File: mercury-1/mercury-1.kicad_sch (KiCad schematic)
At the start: 76 parts, among them J1 +22.2V Logic Battery Array, J2 +14.4V Drivetrain Battery Arr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, J3 +22.2V A/S Battery Array, J4 Jetson, J5 POE Injector, J6 Network Switch, J7 P-20-90-PRO-121-B, J8 P-20-90-PRO-121-B, K1 200A Relay 12V Coil, K2 200A Relay 12V Coil, K3 200A Relay 12V Coil, K4 200A Relay 12V Coil, K5 200A Relay 12V Coil, K6 200A Relay 12V Coil, K7 200A Relay 12V Coil, K8 200A Relay 12V Coil, M1 Yellowjacket 5203, M10 NEO_Brushless_Motor, M2 FGA-32124500-G1166, M3 FGA-32124500-G1166, M4 CN-PA36-38244500-G369, M5 NEO_Brushless_Motor, M6 NEO_Brushless_Motor, M7 NEO_Brushless_Motor, M8 NEO_Brushless_Motor, M9 NEO_Brushless_Motor, SW1 SW_SPDT_321, U1 UVLO Relay, U10 MAX6675 Breakout, U11 MAX6675 Breakout, U12 MAX6675 Breakout, U13 MAX6675 Breakout, U14 MAX6675 Breakout, U15 RoboClaw_2x7A, U16 RoboClaw_2x7A, U18 ODESC_V4.2, U19 ODESC_V4.2, U2 Buck Converter, U20 ODESC_V4.2, U21 ODESC_V4.2, U22 ODESC_V4.2, U23 ODESC_V4.2, U24 5k (8mm Bore), U25 5k (8mm Bore), U26 5k (8mm Bore), U3 Buck Converter, U4 UVLO Relay, U5 Logic Relay, U6 Logic Relay, U7 UVLO Relay, U8 RASPBERRY_PI_4B_4GB, U9 MAX6675 Breakout

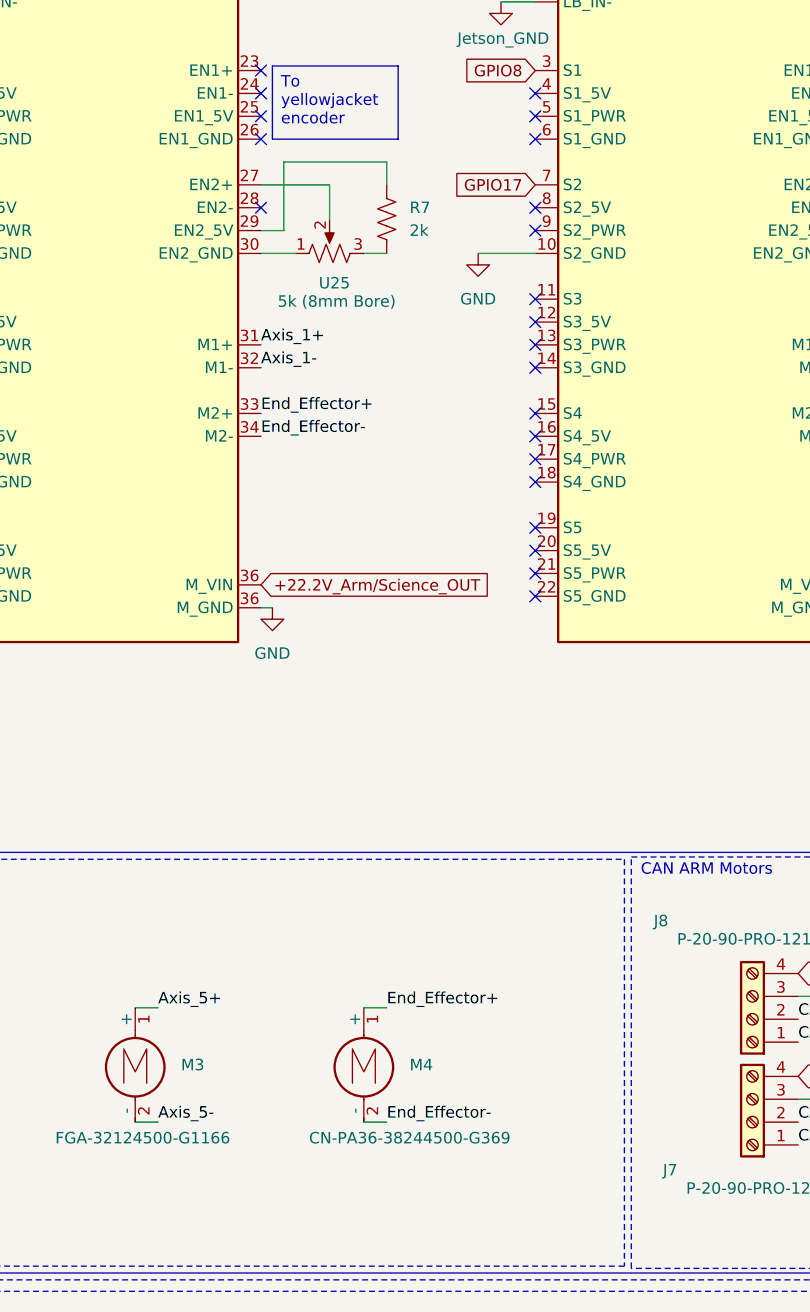
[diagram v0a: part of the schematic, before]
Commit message: changed end effector yo yellowjacket
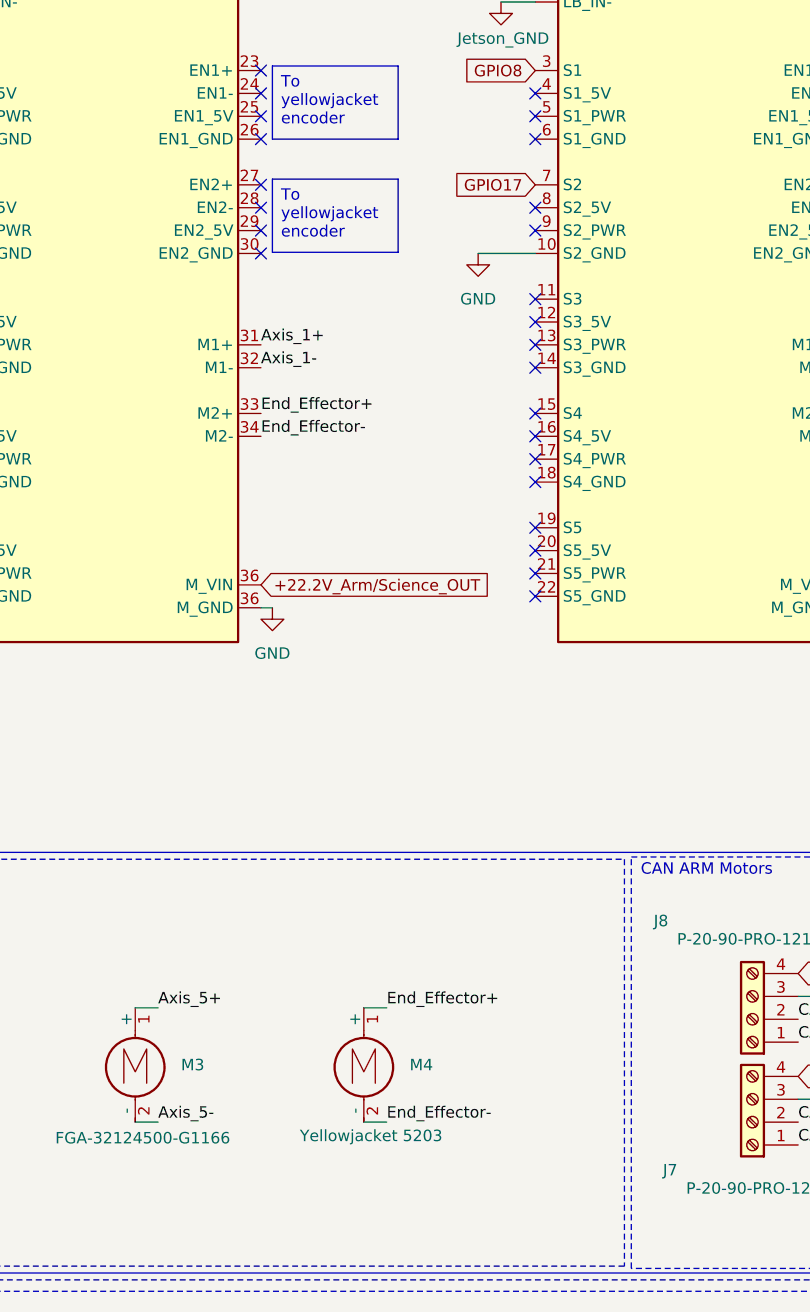
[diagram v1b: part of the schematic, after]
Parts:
- removed M4: CN-PA36-38244500-G369, symbol logic_board:CN-PA36-38244500-G369
- removed R7: 2k, symbol Device:R_US
- removed U25: 5k (8mm Bore), symbol logic_board:NP32HS
- added M4: Yellowjacket 5203, symbol logic_board:Yellowjacket 5203
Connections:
- net End_Effector+: now also M4.1 (+)
- net End_Effector-: now also M4.2 (-)
- no-connect marks 133 -> 136
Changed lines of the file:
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@@
 		)
 	)
+	(text_box "To yellowjacket encoder"
+		(exclude_from_sim no)
+		(at 184.15 283.845 0)
+		(size 13.97 8.128)
+		(margins 0.9525 0.9525 0.9525 0.9525)
+		(stroke
+			(width 0)
+			(type solid)
+		)
+		(fill
+			(type none)
+		)
+		(effects
+			(font
+				(size 1.27 1.27)
+			)
+			(justify left top)
+		)
+	)
 	(text_box "Use this guide to wire using Pyserial"
 		(exclude_from_sim no)
@@
 	)
 	(no_connect
+		(at 182.88 284.48)
+	)
+	(no_connect
 		(at 527.05 254)
 	)
@@
 	)
 	(no_connect
+		(at 182.88 289.56)
+	)
+	(no_connect
 		(at 496.57 212.09)
 	)
@@
 	)
 	(no_connect
+		(at 182.88 292.1)
+	)
+	(no_connect
 		(at 73.025 294.64)
 	)
@@
 		)
 	)
-	(wire
-		(pts
-			(xy 182.88 292.1) (xy 186.69 292.1)
-		)
-		(stroke
-			(width 0)
-			(type default)
-		)
-	)
 	(polyline
 		(pts
@@
 	(wire
 		(pts
-			(xy 182.88 289.56) (xy 185.42 289.56)
-		)
-		(stroke
-			(width 0)
-			(type default)
-		)
-	)
-	(wire
-		(pts
 			(xy 50.8 379.73) (xy 66.04 379.73)
 		)
@@
 	(wire
 		(pts
-			(xy 185.42 281.94) (xy 196.85 281.94)
-		)
-		(stroke
-			(width 0)
-			(type default)
-		)
-	)
-	(wire
-		(pts
 			(xy 199.39 173.99) (xy 208.28 173.99)
 		)
@@
 	(wire
 		(pts
-			(xy 194.31 292.1) (xy 196.85 292.1)
-		)
-		(stroke
-			(width 0)
-			(type default)
-		)
-	)
-	(wire
-		(pts
 			(xy 208.28 66.04) (xy 208.28 81.28)
 		)
@@
 	(wire
 		(pts
-			(xy 190.5 288.29) (xy 190.5 284.48)
-		)
-		(stroke
-			(width 0)
-			(type default)
-		)
-	)
-	(wire
-		(pts
-			(xy 185.42 281.94) (xy 185.42 289.56)
-		)
-		(stroke
-			(width 0)
-			(type default)
-		)
-	)
-	(wire
-		(pts
 			(xy 393.7 30.48) (xy 393.7 33.02)
 		)
@@
 	(wire
 		(pts
-			(xy 190.5 284.48) (xy 182.88 284.48)
-		)
-		(stroke
-			(width 0)
-			(type default)
-		)
-	)
-	(wire
-		(pts
 			(xy 251.46 269.24) (xy 251.46 276.86)
 		)
@@
 	(wire
 		(pts
-			(xy 196.85 281.94) (xy 196.85 284.48)
-		)
-		(stroke
-			(width 0)
-			(type default)
-		)
-	)
-	(wire
-		(pts
 			(xy 248.92 289.56) (xy 251.46 289.56)
 		)
@@
 	)
 	(symbol
+		(lib_id "logic_board:Yellowjacket 5203")
+		(at 194.31 381 0)
+		(unit 1)
+		(exclude_from_sim no)
+		(in_bom yes)
+		(on_board yes)
+		(dnp no)
+		(property "Reference" "M4"
+			(at 199.39 382.2699 0)
+			(effects
+				(font
+					(size 1.27 1.27)
+				)
+				(justify left)
+			)
+		)
+		(property "Value" "Yellowjacket 5203"
+			(at 187.198 390.144 0)
+			(effects
+				(font
+					(size 1.27 1.27)
+				)
+				(justify left)
+			)
+		)
+		(property "Footprint" ""
+			(at 194.31 383.286 0)
+			(effects
+				(font
+					(size 1.27 1.27)
+				)
+				(hide yes)
+			)
+		)
+		(property "Datasheet" "https://www.gobilda.com/5203-series-yellow-jacket-planetary-gear-motor-19-2-1-ratio-24mm-length-8mm-rex-shaft-312-rpm-3-3-5v-encoder/?srsltid=AfmBOop0hJPw3SFHkwtuK_eQ_aN3VPcP46iypOMregJbB3z72pbZtZjr"
+			(at 194.31 383.286 0)
+			(effects
+				(font
+					(size 1.27 1.27)
+				)
+				(hide yes)
+			)
+		)
+		(property "Description" "Yellowjacket 5203"
+			(at 194.31 381 0)
+			(effects
+				(font
+					(size 1.27 1.27)
+				)
+				(hide yes)
+			)
+		)
+		(pin "1"
+		)
+		(pin "2"
+		)
+		(instances
+			(project "mercury-1"
+				(path "/1b548578-061f-412b-9a17-10125f836cd9"
+					(reference "M4")
+					(unit 1)
+				)
+			)
+		)
+	)
+	(symbol
 		(lib_id "logic_board:MAX6675_Breakout")
 		(at 285.75 176.53 0)
@@
 	)
 	(symbol
-		(lib_id "logic_board:NP32HS")
-		(at 190.5 292.1 90)
-		(unit 1)
-		(exclude_from_sim no)
-		(in_bom yes)
-		(on_board yes)
-		(dnp no)
-		(property "Reference" "U25"
-			(at 192.786 295.402 90)
-			(effects
-				(font
-					(size 1.27 1.27)
-				)
-				(justify left)
-			)
-		)
-		(property "Value" "5k (8mm Bore)"
-			(at 197.866 297.434 90)
-			(effects
-				(font
-					(size 1.27 1.27)
-				)
-				(justify left)
-			)
-		)
-		(property "Footprint" ""
-			(at 190.5 292.1 0)
-			(effects
-				(font
-					(size 1.27 1.27)
-				)
-				(hide yes)
-			)
-		)
-		(property "Datasheet" "https://p3america.com/np32hs-series/?searchid=67683&search_query=RH24PC+Series+8mm"
-			(at 190.5 291.846 0)
-			(effects
-				(font
-					(size 1.27 1.27)
-				)
-				(hide yes)
-			)
-		)
-		(property "Description" "5k (8mm Bore)"
-			(at 190.5 292.1 0)
-			(effects
-				(font
-					(size 1.27 1.27)
-				)
-				(hide yes)
-			)
-		)
-		(pin "2"
-		)
-		(pin "1"
-		)
-		(pin "3"
-		)
-		(instances
-			(project ""
-				(path "/1b548578-061f-412b-9a17-10125f836cd9"
-					(reference "U25")
-					(unit 1)
-				)
-			)
-		)
-	)
-	(symbol
 		(lib_id "logic_board:P-17-80-PRO-51-B")
 		(at 237.49 388.62 180)
@@
 	)
 	(symbol
-		(lib_id "Device:R_US")
-		(at 196.85 288.29 0)
-		(unit 1)
-		(exclude_from_sim no)
-		(in_bom yes)
-		(on_board yes)
-		(dnp no)
-		(fields_autoplaced yes)
-		(property "Reference" "R7"
-			(at 199.39 287.0199 0)
-			(effects
-				(font
-					(size 1.27 1.27)
-				)
-				(justify left)
-			)
-		)
-		(property "Value" "2k"
-			(at 199.39 289.5599 0)
-			(effects
-				(font
-					(size 1.27 1.27)
-				)
-				(justify left)
-			)
-		)
-		(property "Footprint" ""
-			(at 197.866 288.544 90)
-			(effects
-				(font
-					(size 1.27 1.27)
-				)
-				(hide yes)
-			)
-		)
-		(property "Datasheet" "~"
-			(at 196.85 288.29 0)
-			(effects
-				(font
-					(size 1.27 1.27)
-				)
-				(hide yes)
-			)
-		)
-		(property "Description" "Resistor, US symbol"
-			(at 196.85 288.29 0)
-			(effects
-				(font
-					(size 1.27 1.27)
-				)
-				(hide yes)
-			)
-		)
-		(pin "2"
-		)
-		(pin "1"
-		)
-		(instances
-			(project ""
-				(path "/1b548578-061f-412b-9a17-10125f836cd9"
-					(reference "R7")
-					(unit 1)
-				)
-			)
-		)
-	)
-	(symbol
 		(lib_id "power:GND")
 		(at 250.19 331.47 0)
@@
 					(unit 1)
 				)
-			)
-		)
-	)
-	(symbol
-		(lib_id "logic_board:CN-PA36-38244500-G369")
-		(at 194.31 381 0)
-		(unit 1)
-		(exclude_from_sim no)
-		(in_bom yes)
-		(on_board yes)
-		(dnp no)
-		(property "Reference" "M4"
-			(at 199.39 382.2699 0)
-			(effects
-				(font
-					(size 1.27 1.27)
-				)
-				(justify left)
-			)
-		)
-		(property "Value" "CN-PA36-38244500-G369"
-			(at 188.214 390.398 0)
-			(effects
-				(font
-					(size 1.27 1.27)
-				)
-				(justify left)
-			)
-		)
-		(property "Footprint" ""
-			(at 194.31 383.286 0)
-			(effects
-				(font
-					(size 1.27 1.27)
-				)
-				(hide yes)
-			)
-		)
-		(property "Datasheet" "https://www.omc-stepperonline.com/brushed-24v-dc-gear-motor-30kg-cm-8-9rpm-w-369-1-planetary-gearbox-pa36-38244500-g369"
-			(at 194.31 383.286 0)
-			(effects
-				(font
-					(size 1.27 1.27)
-				)
-				(hide yes)
-			)
-		)
-		(property "Description" "CN-PA36-38244500-G369"
-			(at 194.31 381 0)
-			(effects
-				(font
-					(size 1.27 1.27)
-				)
-				(hide yes)
-			)
-		)
-		(pin "1"
-		)
-		(pin "2"
-		)
-		(instances
-			(project ""
-				(path "/1b548578-061f-412b-9a17-10125f836cd9"
-					(reference "M4")
-					(unit 1)
-				)

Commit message: Updated Roboclaw wiring and arm connectors.
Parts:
- removed BT2, BT6: +22.2v 10Ah, symbol Device:Battery
- removed J7: P-20-90-PRO-121-B, symbol logic_board:P-17-80-PRO-51-B
- removed J8: P-20-90-PRO-121-B, symbol logic_board:P-20-90-PRO-121-B
- removed R1, R2, R3, R4, R5, R6: 2 (50W), symbol Device:R_US
- removed U26: 5k (8mm Bore), symbol logic_board:NP32HS
- added J10, J11, J12, J13, J8, J9: Andersen Connector, symbol Connector:Screw_Terminal_01x02
- added J14: DB25 Encoder Harness, symbol Connector:DB25_Pins
- added J15: P-20-90-PRO-121-B, symbol Connector:Screw_Terminal_01x02
- added J16: RJ-45 Bulkhead, Connector_RJ:RJ45_Bel_V895-1001-AW_Vertical, symbol logic_board:RJ45_Bel_V895-1001-AW
- added J17: USB_Bulkhead, symbol logic_board:USB_Bulkhead
- added J7: P-17-80-PRO-121-B, symbol Connector:Screw_Terminal_01x02
- added R7: 7.5k, symbol Device:R_US
- added U17: 5k (8mm Bore), symbol logic_board:NP32HS
- R8: value 2k -> 7.5k
- R9: value 2k -> 120
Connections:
- net Axis_1+: now also J11.1 (Pin_1)
- net Axis_1-: now also J11.2 (Pin_2)
- net Axis_4+: now also J9.1 (Pin_1)
- net Axis_4-: now also J9.2 (Pin_2)
- net Axis_5+: now also J10.1 (Pin_1)
- net Axis_5-: now also J10.2 (Pin_2)
- net CAN_H_ARM: now also R9.1, R9.2, J14.21 (P21), J14.9, J15.1 (Pin_1), J15.2 (Pin_2), J7.1 (Pin_1), J7.2 (Pin_2)
- net End_Effector+: now also J12.1 (Pin_1)
- net End_Effector-: now also J12.2 (Pin_2)
- net GND: now also J13.1 (Pin_1), J13.2 (Pin_2)
- net Jetson_+5V: now also U15.1 (LB_IN+), U16.1 (LB_IN+)
- net PI_+5V: no longer U15.1 (LB_IN+), U16.1 (LB_IN+)
- net axis5_PU: now reaches U15.29 (EN2_5V)
- net axis5_PU: now also J14.19 (P19), R7.2; no longer R9.1
- net axis1_CHA: now reaches U16.23 (EN1+)
- net axis1_CHA: now also U16.24 (EN1-), J14.24 (P24)
- net axis1_5V: now reaches U16.25 (EN1_5V)
- net axis1_5V: now also J14.25 (P25)
- net axis1_GND: now reaches U16.26 (EN1_GND)
- net axis1_GND: now also J14.13
- net EF_CHA: now reaches U16.27 (EN2+)
- net EF_CHA: now also J14.22 (P22)
- net EF_CHB: now reaches U16.28 (EN2-)
- net EF_CHB: now also J14.10
- net EF_5V: now reaches U16.29 (EN2_5V)
- net EF_5V: now also J14.23 (P23)
- net EF_GND: now reaches U16.30 (EN2_GND)
- net EF_GND: now also J14.11
- net axis4_AO: now reaches U15.23 (EN1+), U24.2
- net axis4_AO: now also J14.20 (P20)
- net at R8.1: now also U24.3; no longer U15.25 (EN1_5V)
- net axis4_E_GND: now reaches U15.26 (EN1_GND), U24.1
- net axis4_E_GND: now also J14.7
- net axis5_AO: now reaches U15.27 (EN2+)
- net axis5_AO: now also J14.6, U17.2
- net axis5_E_GND: now reaches U15.30 (EN2_GND)
- net axis5_E_GND: now also J14.18 (P18), U17.1
- net axis4_PU: now reaches R8.2
- net axis4_PU: now also U15.25 (EN1_5V), J14.8; no longer U24.3
- removed net +22.2V_Arm/Science_OUT: K8.13, U15.36 (M_GND), U16.36 (M_GND)
- new net: R7.1, U17.3
- new net +22.2V_A/S_OUT: J8.1 (Pin_1), J8.2 (Pin_2), K8.13, U15.36 (M_GND), U16.36 (M_GND)
- new net axis1_CHB: J14.12
- no-connect marks 136 -> 149
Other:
- note added: "Analog Encoders for Axis 4,5"
- note added: "Axis 1,4,5 and EF"
- note added: "CAN ARM Motors (Axis 2,3)"
- note added: "Debug"
- note added: "Front Bulkhead Connectors for Arm/Science"
- note removed: "Axis 1,2,3,4,5 and End Effector"
- note removed: "CAN ARM Motors"
- moved on the sheet: BT1, BT5, R8, U15, U16, U24

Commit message: Updates
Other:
- note removed: "Science"
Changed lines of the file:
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@@
-	)
-	(rectangle
-		(start 426.72 13.97)
-		(end 581.66 138.43)
-		(stroke
-			(width 0)
-			(type dash)
-		)
-		(fill
-			(type none)
-		)
 	)
 	(rectangle
@@
 		)
 	)
-	(text "Science"
-		(exclude_from_sim no)
-		(at 430.784 15.494 0)
-		(effects
-			(font
-				(size 1.27 1.27)
-			)
-		)
-	)
